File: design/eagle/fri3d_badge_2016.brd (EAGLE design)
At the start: 76.5 x 67.4 mm, 45 parts

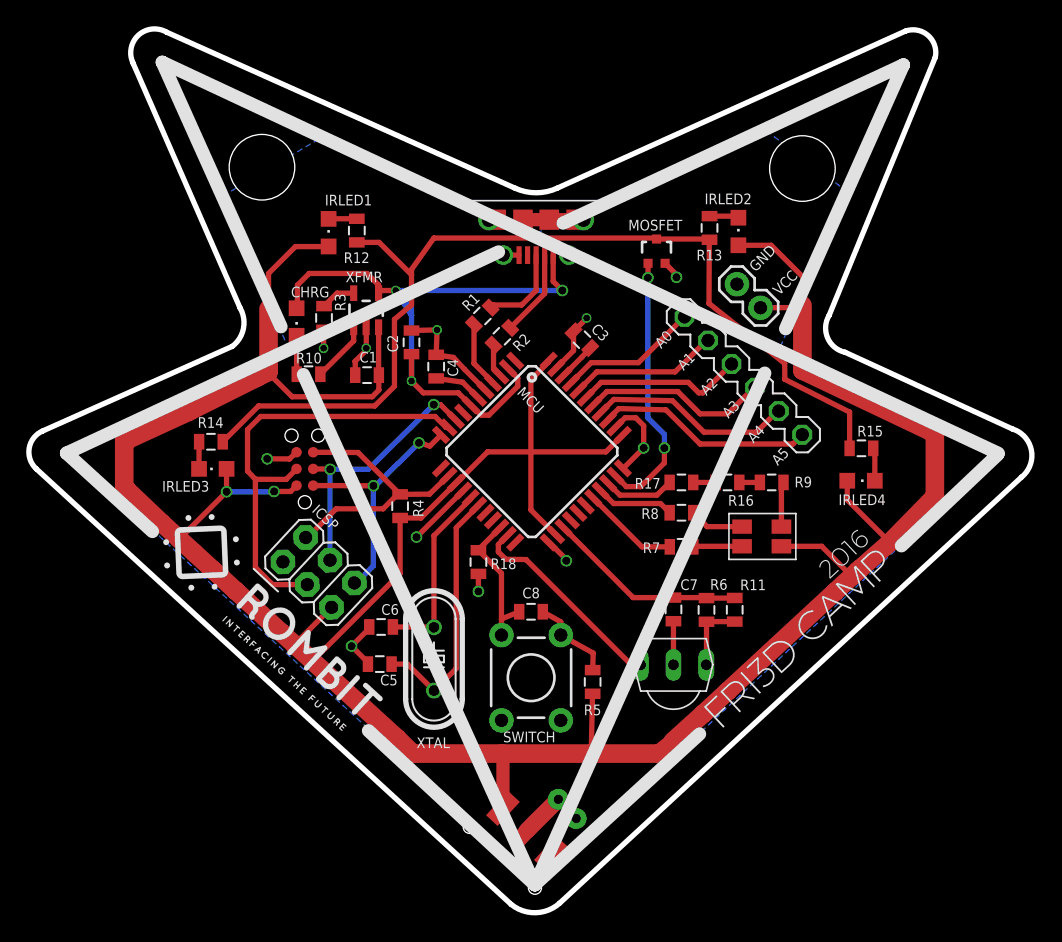
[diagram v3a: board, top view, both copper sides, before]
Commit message: fixed MOSFET footprint + added dots for diodes
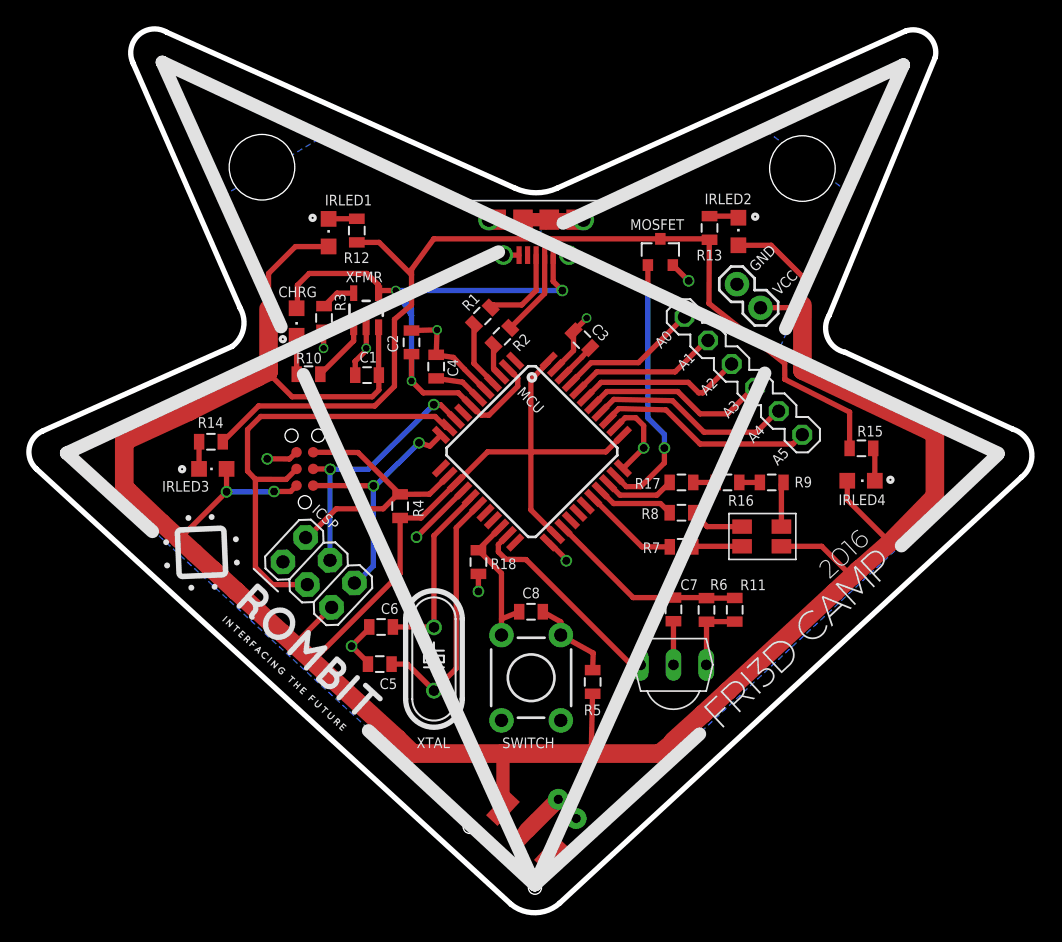
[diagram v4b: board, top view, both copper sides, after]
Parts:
- MOSFET: value MOSFET-NCHANNEL2N7002PW -> N-CHANNEL-MOSFET-BSS138; device SparkFun-DiscreteSemi:SOT323 -> GeekAmmo:SOT23-3
- moved MOSFET 0.30 mm to (49.5, 50.8)
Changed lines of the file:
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@@
 <wire x1="20.78379375" y1="25.3565375" x2="35.535421875" y2="9.53735625" width="0.4064" layer="22"/>
 <text x="41.951934375" y="40.4945" size="1.778" layer="22" rot="MR317">battery</text>
+<circle x="67.01" y="33.47" radius="0.117046875" width="0.4064" layer="25"/>
+<circle x="56.7" y="53.53" radius="0.117046875" width="0.4064" layer="25"/>
+<circle x="22.96" y="53.44" radius="0.117046875" width="0.4064" layer="25"/>
+<circle x="13.01" y="34.28" radius="0.117046875" width="0.4064" layer="25"/>
+<circle x="20.69" y="44.19" radius="0.117046875" width="0.4064" layer="25"/>
 </plain>
 <attributes>
@@
 </element>
 <element name="C5" library="SparkFun-Capacitors" package="0805" value="18pF" x="28.08" y="19.42" smashed="yes">
-<attribute name="NAME" x="28.106575" y="17.799915625" size="0.8128" layer="25"/>
+<attribute name="NAME" x="28.066575" y="17.519915625" size="0.8128" layer="25"/>
 </element>
 <element name="C6" library="SparkFun-Capacitors" package="0805" value="18pF" x="28.18" y="22.25" smashed="yes">
-<attribute name="NAME" x="28.197290625" y="23.176209375" size="0.8128" layer="25"/>
+<attribute name="NAME" x="28.167290625" y="23.246209375" size="0.8128" layer="25"/>
 </element>
 <element name="C7" library="SparkFun-Capacitors" package="0805" value="0.1uF" x="50.47" y="23.59" smashed="yes" rot="R270">
@@
 </element>
 <element name="CHRGLED" library="adafruit" package="CHIPLED_0805" value="CHRG" x="21.74" y="45.5" smashed="yes" rot="R180">
-<attribute name="VALUE" x="21.31" y="47.38" size="0.8128" layer="25"/>
-</element>
-<element name="MOSFET" library="SparkFun-DiscreteSemi" package="SOT323" value="MOSFET-NCHANNEL2N7002PW" x="49.18" y="50.9" smashed="yes">
-<attribute name="PROD_ID" value="TRANS-11151" x="49.18" y="50.9" size="1.778" layer="27" display="off"/>
-<attribute name="NAME" x="47.0245" y="52.478" size="0.8128" layer="25"/>
+<attribute name="VALUE" x="20.35" y="47.39" size="0.8128" layer="25"/>
 </element>
 <element name="R1" library="SparkFun-Passives" package="0805" value="22" x="35.9" y="45.96" smashed="yes" rot="R225">
@@
 <element name="SWITCH" library="SparkFun-Electromechanical" package="TACTILE-PTH" value="SWITCH-MOMENTARY-2PTH" x="39.62" y="18.38" smashed="yes" rot="R270">
 <attribute name="PROD_ID" value=" SWCH-08441" x="39.62" y="18.38" size="1.778" layer="27" rot="R270" display="off"/>
-<attribute name="NAME" x="37.48" y="13.46" size="0.8128" layer="25" ratio="10"/>
+<attribute name="NAME" x="37.41" y="13.01" size="0.8128" layer="25" ratio="10"/>
 </element>
 <element name="MCU" library="SparkFun-DigitalIC" package="TQFP44" value="ATMEGA32U4TQFP-44" x="39.68" y="35.62" smashed="yes" rot="R315">
@@
 <element name="J2" library="SparkFun-Connectors" package="1X02" value="" x="55.31" y="48.38" smashed="yes" rot="R315">
 <attribute name="VALUE" x="52.166909375" y="47.032959375" size="1.27" layer="27" rot="R315"/>
+</element>
+<element name="MOSFET" library="GeekAmmo" package="SOT23-3" value="N-CHANNEL-MOSFET-BSS138" x="49.47" y="50.84" smashed="yes">
+<attribute name="DIGIKEY" value="BSS138TR-ND" x="49.47" y="50.84" size="1.778" layer="27" display="off"/>
+<attribute name="OTHER" value="" x="49.47" y="50.84" size="1.778" layer="27" display="off"/>
+<attribute name="ELEMENT14" value="2323154" x="49.47" y="50.84" size="1.778" layer="27" display="off"/>
+<attribute name="URL" value="http://au.element14.com/fairchild-semiconductor/bss138/mosfet-n-ch-50v-220ma-sot-23/dp/2323154" x="49.47" y="50.84" size="1.778" layer="27" display="off"/>
+<attribute name="DATASHEET" value="http://www.fairchildsemi.com/ds/BS/BSS138.pdf" x="49.47" y="50.84" size="1.778" layer="27" display="off"/>
+<attribute name="NAME" x="47.165" y="52.525" size="0.8128" layer="25"/>
 </element>
 </elements>
@@
 <contactref element="U$3" pad="GND"/>
 <contactref element="C7" pad="2"/>
-<contactref element="MOSFET" pad="2"/>
 <via x="43.85" y="45.8" extent="1-16" drill="0.5"/>
 <wire x1="36.144465625" y1="40.286903125" x2="34.544975" y2="41.88639375" width="0.4064" layer="1"/>
@@
 <wire x1="27.18" y1="19.42" x2="27.18" y2="19.54" width="0.4064" layer="1"/>
 <wire x1="27.18" y1="19.54" x2="25.93" y2="20.79" width="0.4064" layer="1"/>
-<wire x1="49.83" y1="49.975" x2="50.7" y2="49.105" width="0.4064" layer="1"/>
-<wire x1="50.7" y1="49.105" x2="50.7" y2="48.91" width="0.4064" layer="1"/>
-<via x="50.7" y="48.91" extent="1-16" drill="0.6"/>
+<contactref element="MOSFET" pad="2"/>
+<wire x1="50.42" y1="49.84" x2="51.62" y2="48.64" width="0.4064" layer="1"/>
+<wire x1="51.62" y1="48.64" x2="51.63" y2="48.64" width="0.4064" layer="1"/>
+<via x="51.63" y="48.64" extent="1-16" drill="0.6"/>
 </signal>
 <signal name="D+">
@@
 </signal>
 <signal name="IR_TX">
-<contactref element="MOSFET" pad="1"/>
 <contactref element="MCU" pad="32"/>
 <wire x1="46.043959375" y1="33.781521875" x2="46.87548125" y2="32.95" width="0.4064" layer="1"/>
@@
 <via x="49.78" y="35.89" extent="1-16" drill="0.6"/>
 <wire x1="49.78" y1="36.93" x2="48.52" y2="38.19" width="0.4064" layer="16"/>
-<wire x1="48.52" y1="38.19" x2="48.52" y2="48.87" width="0.4064" layer="16"/>
-<via x="48.52" y="48.87" extent="1-16" drill="0.6"/>
-<wire x1="48.52" y1="48.87" x2="48.53" y2="48.88" width="0.4064" layer="1"/>
-<wire x1="48.53" y1="48.88" x2="48.53" y2="49.975" width="0.4064" layer="1"/>
+<wire x1="48.52" y1="38.19" x2="48.52" y2="47.93" width="0.4064" layer="16"/>
+<via x="48.52" y="47.93" extent="1-16" drill="0.6"/>
 <wire x1="49.78" y1="36.93" x2="49.78" y2="35.89" width="0.4064" layer="16"/>
 <wire x1="49.78" y1="34.76" x2="49.78" y2="35.89" width="0.4064" layer="1"/>
+<contactref element="MOSFET" pad="1"/>
+<wire x1="48.52" y1="49.84" x2="48.52" y2="47.93" width="0.4064" layer="1"/>
 </signal>
 <signal name="BUTTON">
@@
 <contactref element="R14" pad="1"/>
 <contactref element="R13" pad="1"/>
-<contactref element="MOSFET" pad="3"/>
 <contactref element="R12" pad="1"/>
 <wire x1="29.2" y1="45.7" x2="30.5" y2="46.8" width="0.4064" layer="1"/>
@@
 <wire x1="30.5" y1="49.1" x2="28.03" y2="51.57" width="0.4064" layer="1"/>
 <wire x1="28.03" y1="51.57" x2="26.33" y2="51.57" width="0.4064" layer="1"/>
-<wire x1="49.055" y1="51.9" x2="32.2" y2="51.9" width="0.4064" layer="1"/>
-<wire x1="32.2" y1="51.9" x2="30.5" y2="49.5" width="0.4064" layer="1"/>
+<wire x1="32.2" y1="51.84" x2="30.5" y2="49.5" width="0.4064" layer="1"/>
 <wire x1="30.5" y1="49.5" x2="30.5" y2="49.1" width="0.4064" layer="1"/>
 <wire x1="16.11" y1="36.37" x2="16.14" y2="36.4" width="0.4064" layer="1"/>
@@
 <wire x1="27.7" y1="39.1" x2="18.84" y2="39.1" width="0.4064" layer="1"/>
 <wire x1="18.84" y1="39.1" x2="16.11" y2="36.37" width="0.4064" layer="1"/>
-<wire x1="49.055" y1="51.9" x2="49.18" y2="51.825" width="0.4064" layer="1"/>
-<wire x1="49.18" y1="51.825" x2="53.165" y2="51.825" width="0.4064" layer="1"/>
 <wire x1="53.165" y1="51.825" x2="53.22" y2="51.77" width="0.4064" layer="1"/>
 <wire x1="63.9" y1="35.87" x2="63.9" y2="38.63" width="0.4064" layer="1"/>
@@
 <wire x1="53.18" y1="46.91" x2="53.2" y2="51.75" width="0.4064" layer="1"/>
 <wire x1="53.2" y1="51.75" x2="53.22" y2="51.77" width="0.4064" layer="1"/>
+<contactref element="MOSFET" pad="3"/>
+<wire x1="32.2" y1="51.84" x2="49.47" y2="51.84" width="0.4064" layer="1"/>
+<wire x1="49.47" y1="51.84" x2="53.22" y2="51.84" width="0.4064" layer="1"/>
+<wire x1="53.22" y1="51.84" x2="53.22" y2="51.77" width="0.4064" layer="1"/>
 </signal>
 <signal name="N$3">

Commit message: added header for IR_TX
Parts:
- added IR_TX: (no value), SparkFun-Connectors:1X01
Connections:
- net N$24: now also IR_TX.1
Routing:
- net N$24: track 75.4 -> 78.6 mm
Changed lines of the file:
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@@
 <attribute name="NAME" x="47.165" y="52.525" size="0.8128" layer="25"/>
+</element>
+<element name="IR_TX" library="SparkFun-Connectors" package="1X01" value="" x="49.5" y="55.04" smashed="yes">
+<attribute name="NAME" x="51.1838" y="55.5888" size="0.8128" layer="25" rot="R23"/>
+<attribute name="VALUE" x="48.23" y="51.865" size="1.27" layer="27"/>
 </element>
 </elements>
@@
 <wire x1="49.47" y1="51.84" x2="53.22" y2="51.84" width="0.4064" layer="1"/>
 <wire x1="53.22" y1="51.84" x2="53.22" y2="51.77" width="0.4064" layer="1"/>
+<contactref element="IR_TX" pad="1"/>
+<wire x1="49.47" y1="51.84" x2="49.5" y2="51.87" width="0.4064" layer="1"/>
+<wire x1="49.5" y1="51.87" x2="49.5" y2="55.04" width="0.4064" layer="1"/>
 </signal>
 <signal name="N$3">

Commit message: moved IR_TX test header
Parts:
- moved IR_TX 19.8 mm to (29.8, 53.0)
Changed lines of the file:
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@@
 <attribute name="NAME" x="47.165" y="52.525" size="0.8128" layer="25"/>
 </element>
-<element name="IR_TX" library="SparkFun-Connectors" package="1X01" value="" x="49.5" y="55.04" smashed="yes">
-<attribute name="NAME" x="51.1838" y="55.5888" size="0.8128" layer="25" rot="R23"/>
-<attribute name="VALUE" x="48.23" y="51.865" size="1.27" layer="27"/>
+<element name="IR_TX" library="SparkFun-Connectors" package="1X01" value="" x="29.77" y="53.05" smashed="yes">
+<attribute name="NAME" x="31.7338" y="52.6988" size="0.8128" layer="25"/>
+<attribute name="VALUE" x="28.5" y="49.875" size="1.27" layer="27"/>
 </element>
 </elements>
@@
 <wire x1="30.5" y1="49.1" x2="28.03" y2="51.57" width="0.4064" layer="1"/>
 <wire x1="28.03" y1="51.57" x2="26.33" y2="51.57" width="0.4064" layer="1"/>
-<wire x1="32.2" y1="51.84" x2="30.5" y2="49.5" width="0.4064" layer="1"/>
+<wire x1="32.2" y1="51.84" x2="32.05539375" y2="51.640953125" width="0.4064" layer="1"/>
+<wire x1="32.05539375" y1="51.640953125" x2="30.5" y2="49.5" width="0.4064" layer="1"/>
 <wire x1="30.5" y1="49.5" x2="30.5" y2="49.1" width="0.4064" layer="1"/>
 <wire x1="16.11" y1="36.37" x2="16.14" y2="36.4" width="0.4064" layer="1"/>
@@
 <contactref element="IR_TX" pad="1"/>
 <wire x1="49.47" y1="51.84" x2="49.5" y2="51.87" width="0.4064" layer="1"/>
-<wire x1="49.5" y1="51.87" x2="49.5" y2="55.04" width="0.4064" layer="1"/>
+<wire x1="29.77" y1="53.05" x2="32.05539375" y2="51.640953125" width="0.4064" layer="1"/>
 </signal>
 <signal name="N$3">
